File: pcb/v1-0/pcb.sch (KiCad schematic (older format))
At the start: 30 parts, among them J1 10118194-0001LF, J2 Conn_02x02_Odd_Even, J3 Conn_02x03_Odd_Even, J4 Conn_01x01, J5 Conn_01x04, J6 Conn_01x04, U1 ATtiny3216-S, U2 SI7211-B-00-IV

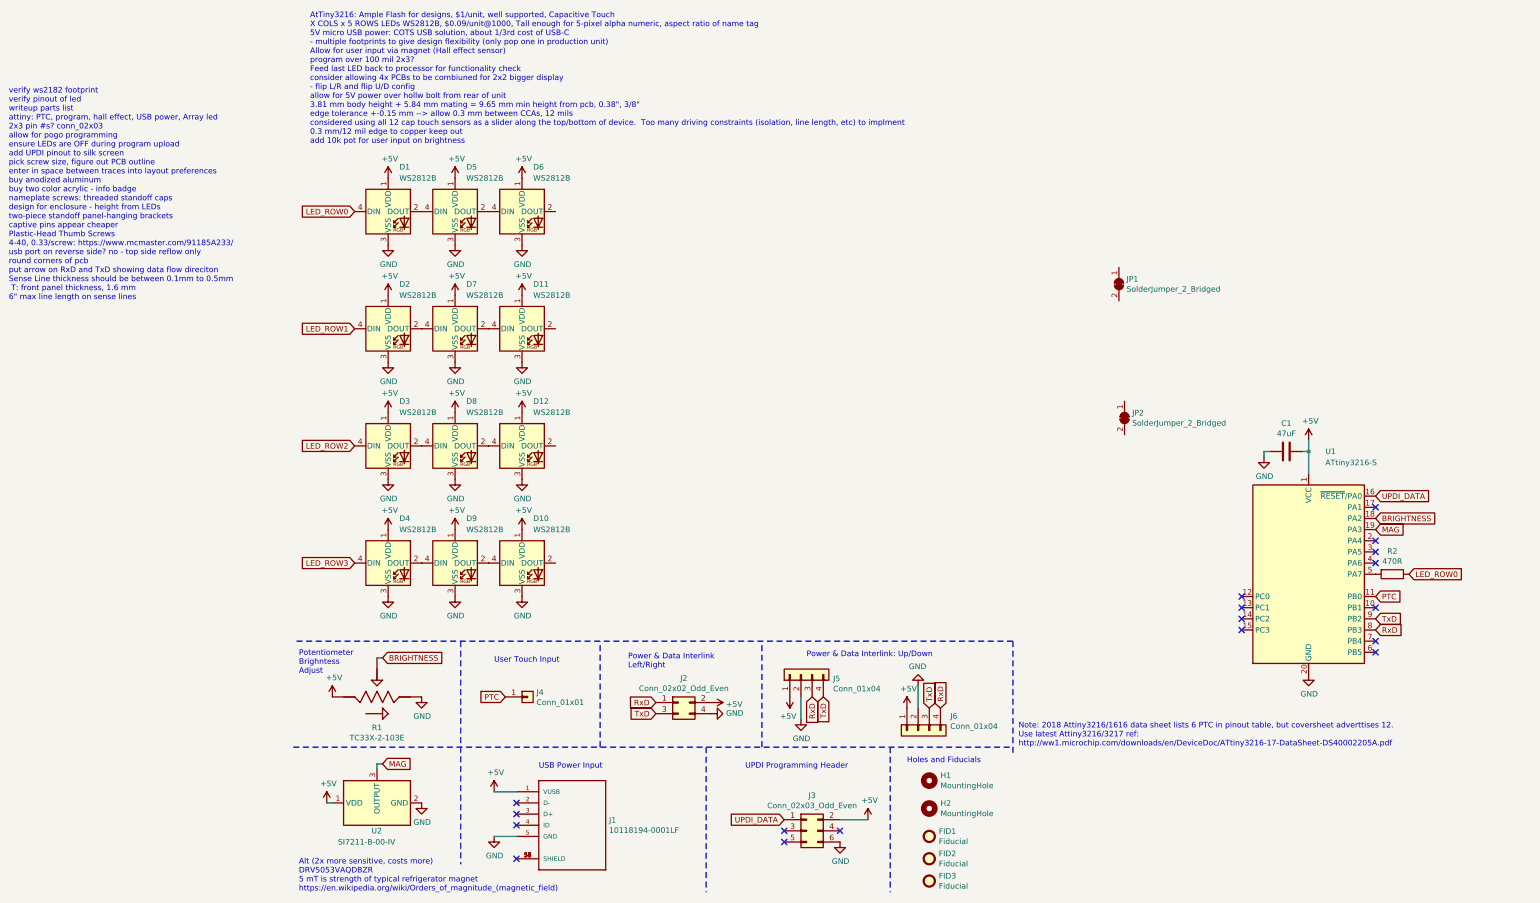
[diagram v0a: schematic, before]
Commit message: copy-paste LEDs in schematic
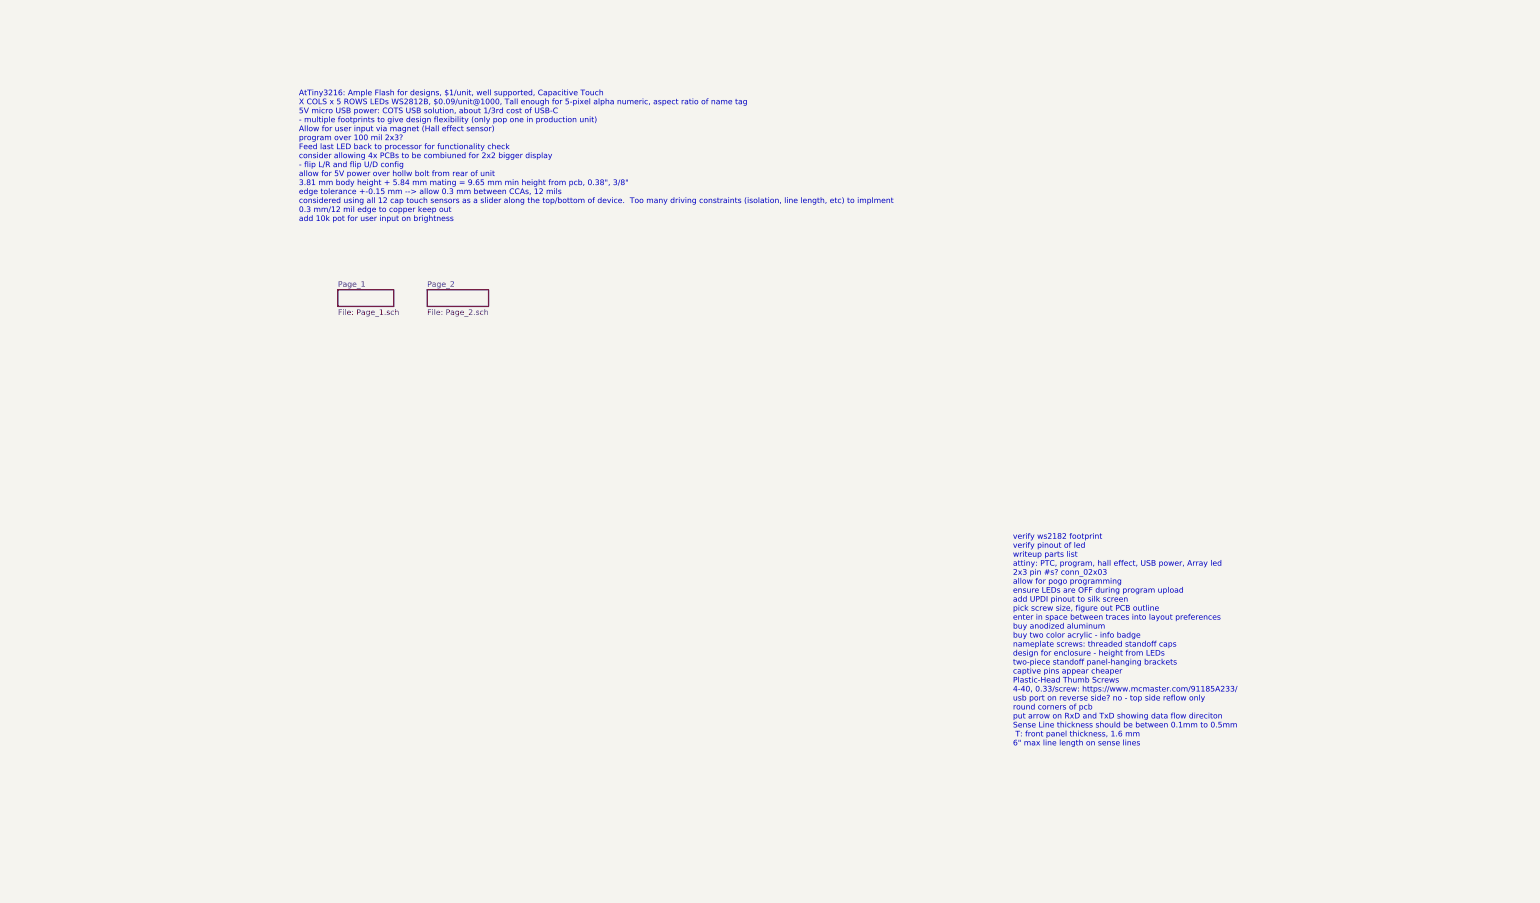
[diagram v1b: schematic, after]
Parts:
- removed C1: 47uF, Capacitor_SMD:C_0805_2012Metric, symbol Device:C
- removed D1, D10, D11, D12, D2, D3, D4, D5, D6, D7, D8, D9: WS2812B, WS2812B:LED_WS2812B_PLCC4_5.0x5.0mm_P3.2mm, symbol LED:WS2812B
- removed FID1, FID2, FID3: Fiducial, Fiducial:Fiducial_1mm_Mask2mm, symbol Mechanical:Fiducial
- removed H1, H2: MountingHole, MountingHole:MountingHole_2.5mm, symbol Mechanical:MountingHole
- removed J1: 10118194-0001LF, microUSB:AMPHENOL_10118194-0001LF, symbol microUSB:10118194-0001LF
- removed J2: Conn_02x02_Odd_Even, Connector_PinHeader_2.54mm:PinHeader_2x02_P2.54mm_Vertical, symbol Connector_Generic:Conn_02x02_Odd_Even
- removed J3: Conn_02x03_Odd_Even, Connector_PinHeader_2.54mm:PinHeader_2x03_P2.54mm_Vertical_SMD, symbol Connector_Generic:Conn_02x03_Odd_Even
- removed J4: Conn_01x01, PTC:cap_touch, symbol Connector_Generic:Conn_01x01
- removed J5, J6: Conn_01x04, Connector_PinHeader_2.54mm:PinHeader_1x04_P2.54mm_Vertical, symbol Connector_Generic:Conn_01x04
- removed JP1, JP2: SolderJumper_2_Bridged, Jumper:SolderJumper-2_P1.3mm_Bridged_RoundedPad1.0x1.5mm, symbol Jumper:SolderJumper_2_Bridged
- removed R1: TC33X-2-103E, TC33X-2-103E:35WR, symbol TC33X-2-103E:TC33X-2-103E
- removed R2: 470R, Resistor_SMD:R_0805_2012Metric, symbol Device:R
- removed U1: ATtiny3216-S, Package_SO:SOIC-20W_7.5x12.8mm_P1.27mm, symbol MCU_Microchip_ATtiny:ATtiny3216-S
- removed U2: SI7211-B-00-IV, Package_TO_SOT_SMD:SC-59, symbol Sensor_Magnetic:AH1806-W
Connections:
- no-connect marks 18 -> 0
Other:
- note removed: "Alt (2x more sensitive, costs more)\nDRV5053VAQDBZR\n5 mT is strength of typical refrigerator magnet\nhttps://en.wikipedia.org/wiki/Orders_of_magnitude_(magnetic_field)"
- note removed: "Holes and Fiducials"
- note removed: "Note: 2018 Attiny3216/1616 data sheet lists 6 PTC in pinout table, but coversheet adverttises 12.\nUse latest Attiny3216/3217 ref:\nhttp://ww1.microchip.com/downloads/en/DeviceDoc/ATtiny3216-17-DataSheet-DS40002205A.pdf"
- note removed: "Potentiometer\nBrighntess\nAdjust"
- note removed: "Power & Data Interlink: Up/Down"
- note removed: "Power & Data Interlink\nLeft/Right"
- note removed: "UPDI Programming Header"
- note removed: "USB Power Input"
- note removed: "User Touch Input"

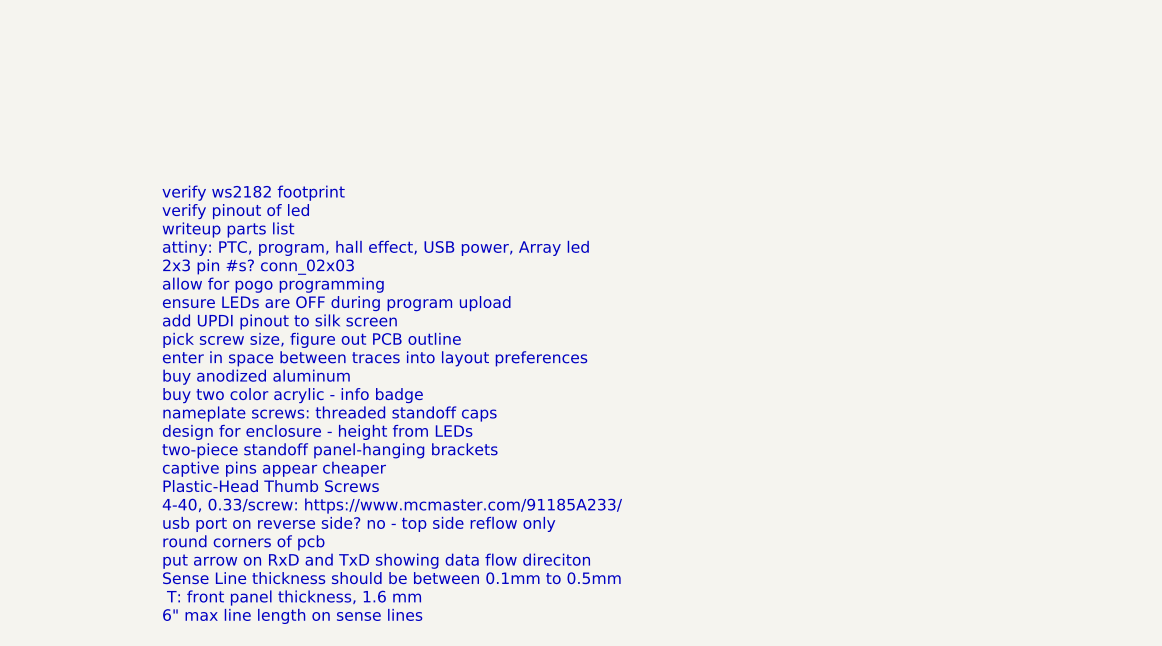
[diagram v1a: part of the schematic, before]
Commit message: link schematic leds to layout
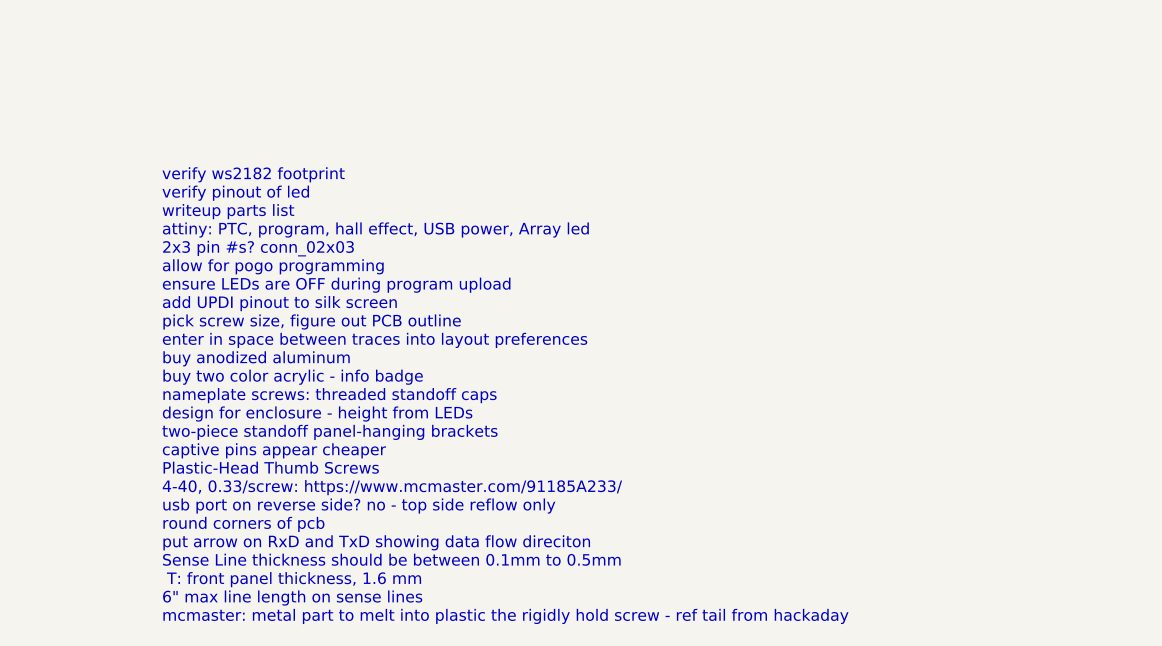
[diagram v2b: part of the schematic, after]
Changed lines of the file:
@@
 $EndDescr
 Text Notes 6950 6450 0    50   ~ 0
-verify ws2182 footprint\nverify pinout of led\nwriteup parts list\nattiny: PTC, program, hall effect, USB power, Array led\n2x3 pin #s? conn_02x03\nallow for pogo programming\nensure LEDs are OFF during program upload\nadd UPDI pinout to silk screen\npick screw size, figure out PCB outline\nenter in space between traces into layout preferences\nbuy anodized aluminum\nbuy two color acrylic - info badge\nnameplate screws: threaded standoff caps\ndesign for enclosure - height from LEDs\ntwo-piece standoff panel-hanging brackets\ncaptive pins appear cheaper\nPlastic-Head Thumb Screws\n4-40, 0.33/screw: https://www.mcmaster.com/91185A233/\nusb port on reverse side? no - top side reflow only\nround corners of pcb\nput arrow on RxD and TxD showing data flow direciton\nSense Line thickness should be between 0.1mm to 0.5mm\n T: front panel thickness, 1.6 mm\n6" max line length on sense lines
+verify ws2182 footprint\nverify pinout of led\nwriteup parts list\nattiny: PTC, program, hall effect, USB power, Array led\n2x3 pin #s? conn_02x03\nallow for pogo programming\nensure LEDs are OFF during program upload\nadd UPDI pinout to silk screen\npick screw size, figure out PCB outline\nenter in space between traces into layout preferences\nbuy anodized aluminum\nbuy two color acrylic - info badge\nnameplate screws: threaded standoff caps\ndesign for enclosure - height from LEDs\ntwo-piece standoff panel-hanging brackets\ncaptive pins appear cheaper\nPlastic-Head Thumb Screws\n4-40, 0.33/screw: https://www.mcmaster.com/91185A233/\nusb port on reverse side? no - top side reflow only\nround corners of pcb\nput arrow on RxD and TxD showing data flow direciton\nSense Line thickness should be between 0.1mm to 0.5mm\n T: front panel thickness, 1.6 mm\n6" max line length on sense lines\nmcmaster: metal part to melt into plastic the rigidly hold screw - ref tail from hackaday
 Text Notes 550  1750 0    50   ~ 0
 AtTiny3216: Ample Flash for designs, $1/unit, well supported, Capacitive Touch\nX COLS x 5 ROWS LEDs WS2812B, $0.09/unit@1000, Tall enough for 5-pixel alpha numeric, aspect ratio of name tag\n5V micro USB power: COTS USB solution, about 1/3rd cost of USB-C\n- multiple footprints to give design flexibility (only pop one in production unit)\nAllow for user input via magnet (Hall effect sensor)\nprogram over 100 mil 2x3?\nFeed last LED back to processor for functionality check\nconsider allowing 4x PCBs to be combiuned for 2x2 bigger display\n- flip L/R and flip U/D config\nallow for 5V power over hollw bolt from rear of unit\n3.81 mm body height + 5.84 mm mating = 9.65 mm min height from pcb, 0.38", 3/8"\nedge tolerance +-0.15 mm --> allow 0.3 mm between CCAs, 12 mils\nconsidered using all 12 cap touch sensors as a slider along the top/bottom of device.  Too many driving constraints (isolation, line length, etc) to implment\n0.3 mm/12 mil edge to copper keep out\nadd 10k pot for user input on brightness

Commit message: compontnets placedr
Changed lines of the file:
@@
 verify ws2182 footprint\nverify pinout of led\nwriteup parts list\nattiny: PTC, program, hall effect, USB power, Array led\n2x3 pin #s? conn_02x03\nallow for pogo programming\nensure LEDs are OFF during program upload\nadd UPDI pinout to silk screen\npick screw size, figure out PCB outline\nenter in space between traces into layout preferences\nbuy anodized aluminum\nbuy two color acrylic - info badge\nnameplate screws: threaded standoff caps\ndesign for enclosure - height from LEDs\ntwo-piece standoff panel-hanging brackets\ncaptive pins appear cheaper\nPlastic-Head Thumb Screws\n4-40, 0.33/screw: https://www.mcmaster.com/91185A233/\nusb port on reverse side? no - top side reflow only\nround corners of pcb\nput arrow on RxD and TxD showing data flow direciton\nSense Line thickness should be between 0.1mm to 0.5mm\n T: front panel thickness, 1.6 mm\n6" max line length on sense lines\nmcmaster: metal part to melt into plastic the rigidly hold screw - ref tail from hackaday
 Text Notes 550  1750 0    50   ~ 0
-AtTiny3216: Ample Flash for designs, $1/unit, well supported, Capacitive Touch\nX COLS x 5 ROWS LEDs WS2812B, $0.09/unit@1000, Tall enough for 5-pixel alpha numeric, aspect ratio of name tag\n5V micro USB power: COTS USB solution, about 1/3rd cost of USB-C\n- multiple footprints to give design flexibility (only pop one in production unit)\nAllow for user input via magnet (Hall effect sensor)\nprogram over 100 mil 2x3?\nFeed last LED back to processor for functionality check\nconsider allowing 4x PCBs to be combiuned for 2x2 bigger display\n- flip L/R and flip U/D config\nallow for 5V power over hollw bolt from rear of unit\n3.81 mm body height + 5.84 mm mating = 9.65 mm min height from pcb, 0.38", 3/8"\nedge tolerance +-0.15 mm --> allow 0.3 mm between CCAs, 12 mils\nconsidered using all 12 cap touch sensors as a slider along the top/bottom of device.  Too many driving constraints (isolation, line length, etc) to implment\n0.3 mm/12 mil edge to copper keep out\nadd 10k pot for user input on brightness
+AtTiny3216: Ample Flash for designs, $1/unit, well supported, Capacitive Touch\nX COLS x 5 ROWS LEDs WS2812B, $0.09/unit@1000, Tall enough for 5-pixel alpha numeric, aspect ratio of name tag\n5V micro USB power: COTS USB solution, about 1/3rd cost of USB-C\n- multiple footprints to give design flexibility (only pop one in production unit)\nAllow for user input via magnet (Hall effect sensor)\nprogram over 100 mil 2x3?\nFeed last LED back to processor for functionality check\nconsider allowing 4x PCBs to be combiuned for 2x2 bigger display\n- flip L/R and flip U/D config\nallow for 5V power over hollw bolt from rear of unit\n3.81 mm body height + 5.84 mm mating = 9.65 mm min height from pcb, 0.38", 3/8"\nedge tolerance +-0.15 mm --> allow 0.3 mm between CCAs, 12 mils\nconsidered using all 12 cap touch sensors as a slider along the top/bottom of device.  Too many driving constraints (isolation, line length, etc) to implment\n0.3 mm/12 mil edge to copper keep out\nadd 10k pot for user input on brightness\nprogram "over USB" (use ID pin on USB as UPDI) https://www.digikey.com/product-detail/en/adafruit-industries-llc/3972/1528-2796-ND/9826284
 $Sheet
 S 900  2350 500  150

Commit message: candidate draft
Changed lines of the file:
@@
 $EndDescr
 Text Notes 6950 6450 0    50   ~ 0
-verify ws2182 footprint\nverify pinout of led\nwriteup parts list\nattiny: PTC, program, hall effect, USB power, Array led\n2x3 pin #s? conn_02x03\nallow for pogo programming\nensure LEDs are OFF during program upload\nadd UPDI pinout to silk screen\npick screw size, figure out PCB outline\nenter in space between traces into layout preferences\nbuy anodized aluminum\nbuy two color acrylic - info badge\nnameplate screws: threaded standoff caps\ndesign for enclosure - height from LEDs\ntwo-piece standoff panel-hanging brackets\ncaptive pins appear cheaper\nPlastic-Head Thumb Screws\n4-40, 0.33/screw: https://www.mcmaster.com/91185A233/\nusb port on reverse side? no - top side reflow only\nround corners of pcb\nput arrow on RxD and TxD showing data flow direciton\nSense Line thickness should be between 0.1mm to 0.5mm\n T: front panel thickness, 1.6 mm\n6" max line length on sense lines\nmcmaster: metal part to melt into plastic the rigidly hold screw - ref tail from hackaday
+verify ws2182 footprint\nverify pinout of led\nwriteup parts list\nattiny: PTC, program, hall effect, USB power, Array led\n2x3 pin #s? conn_02x03\nallow for pogo programming\nensure LEDs are OFF during program upload\nadd UPDI pinout to silk screen\npick screw size, figure out PCB outline\nenter in space between traces into layout preferences\nbuy anodized aluminum\nbuy two color acrylic - info badge\nnameplate screws: threaded standoff caps\ndesign for enclosure - height from LEDs\ntwo-piece standoff panel-hanging brackets\ncaptive pins appear cheaper\nPlastic-Head Thumb Screws\n4-40, 0.33/screw: https://www.mcmaster.com/91185A233/\nusb port on reverse side? no - top side reflow only\nround corners of pcb\nput arrow on RxD and TxD showing data flow direciton\nSense Line thickness should be between 0.1mm to 0.5mm\n T: front panel thickness, 1.6 mm\n6" max line length on sense lines\nmcmaster: metal part to melt into plastic the rigidly hold screw - ref tail from hackaday\nupdate silk screen info
 Text Notes 550  1750 0    50   ~ 0
 AtTiny3216: Ample Flash for designs, $1/unit, well supported, Capacitive Touch\nX COLS x 5 ROWS LEDs WS2812B, $0.09/unit@1000, Tall enough for 5-pixel alpha numeric, aspect ratio of name tag\n5V micro USB power: COTS USB solution, about 1/3rd cost of USB-C\n- multiple footprints to give design flexibility (only pop one in production unit)\nAllow for user input via magnet (Hall effect sensor)\nprogram over 100 mil 2x3?\nFeed last LED back to processor for functionality check\nconsider allowing 4x PCBs to be combiuned for 2x2 bigger display\n- flip L/R and flip U/D config\nallow for 5V power over hollw bolt from rear of unit\n3.81 mm body height + 5.84 mm mating = 9.65 mm min height from pcb, 0.38", 3/8"\nedge tolerance +-0.15 mm --> allow 0.3 mm between CCAs, 12 mils\nconsidered using all 12 cap touch sensors as a slider along the top/bottom of device.  Too many driving constraints (isolation, line length, etc) to implment\n0.3 mm/12 mil edge to copper keep out\nadd 10k pot for user input on brightness\nprogram "over USB" (use ID pin on USB as UPDI) https://www.digikey.com/product-detail/en/adafruit-industries-llc/3972/1528-2796-ND/9826284
